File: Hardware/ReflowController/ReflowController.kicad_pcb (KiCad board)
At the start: 4 copper layers, 160 x 100 mm, 151 parts, among them J101 2060-1452, J102 2060-1452, J103 2060-1453, J104 2060-1452, J105 2060-1452, J106 2060-1452, J107 2060-1452, J108 2060-1452, J109 2060-1452, J110 2060-1452, J111 2060-1452, J112 2060-1452, J601 LCD_HEADER, Q601 BC848, SW601 RotaryEncoder_Switch, SW602 SW_UP, SW603 SW_DOWN, SW604 SW_LEFT, SW605 SW_RIGHT, SW606 SW_SELECT, SW607 SW_RET, SW608 SW_RESET, U301 TSR_1-2450, U302 LD1117S33TR_SOT223, U401 MAX31865xAP, U501 TB67H400AFNG, U601 PI4IOE5V6416, U701 VNQ5160K-E, U702 SZNUD3124DMT1G

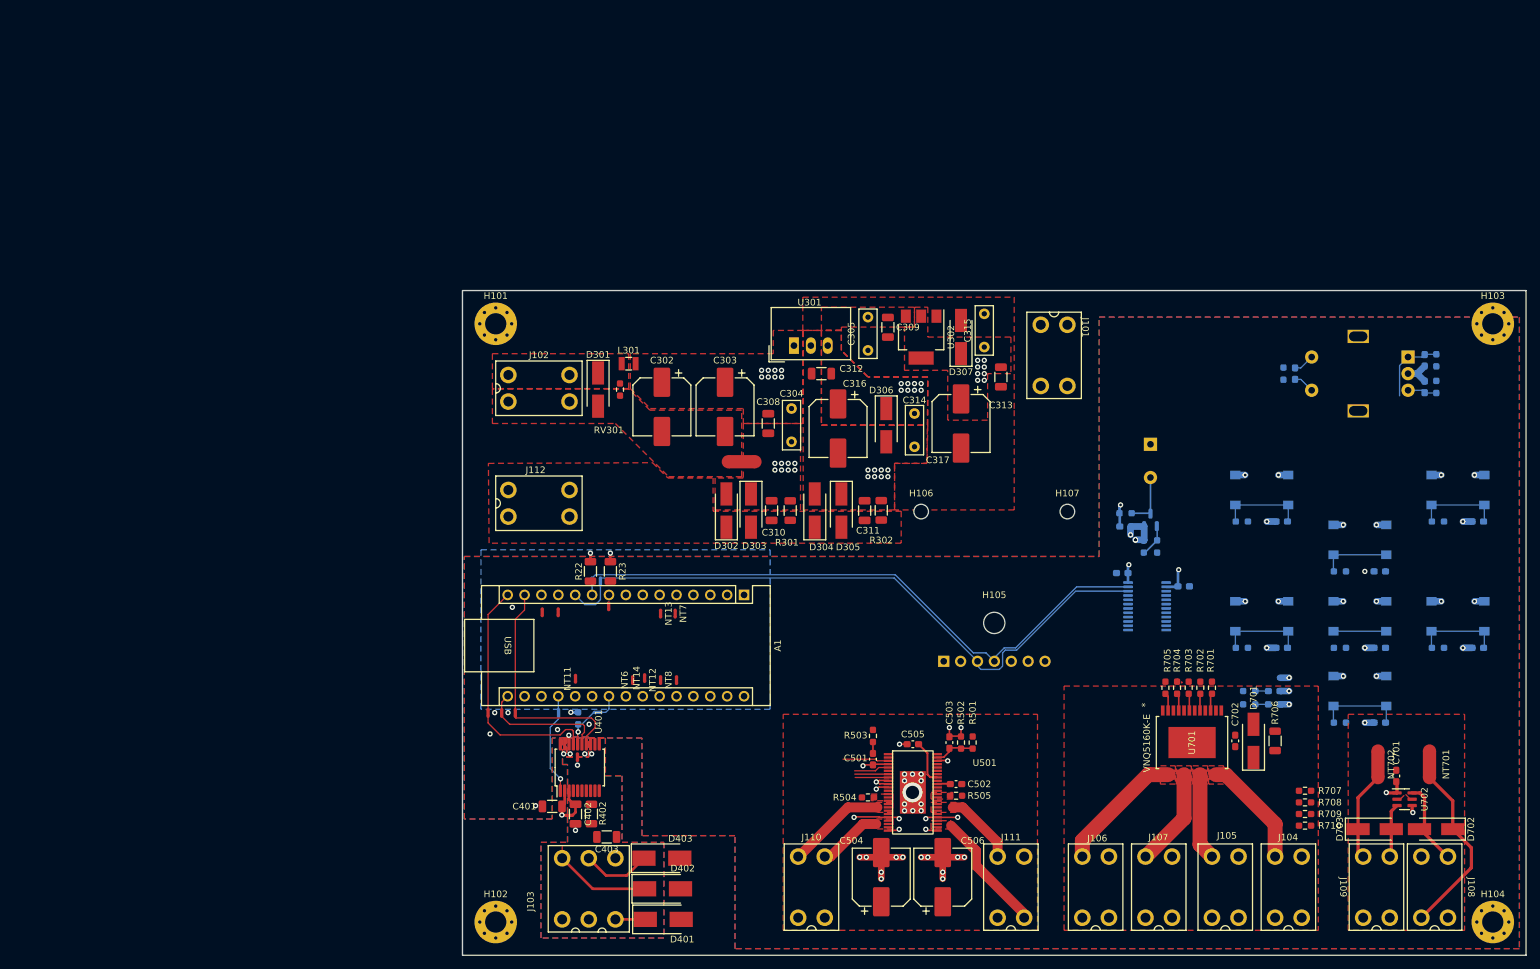
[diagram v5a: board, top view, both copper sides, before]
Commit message: work on +24V power
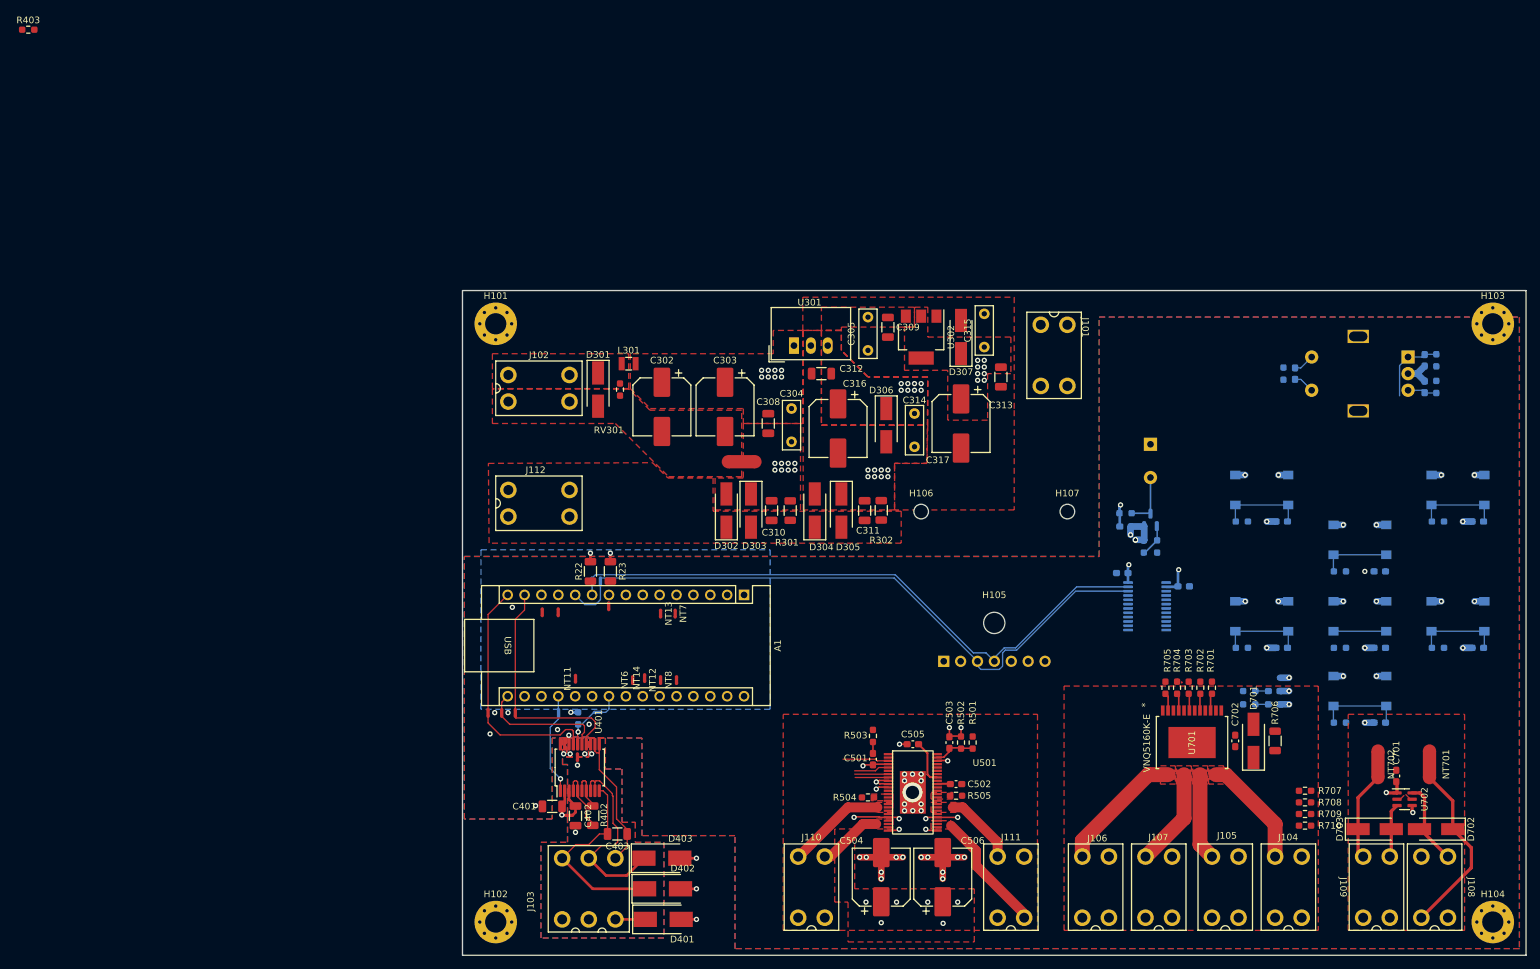
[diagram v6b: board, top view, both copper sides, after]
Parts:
- added R403: 10M, Resistor_SMD:R_0603_1608Metric_Pad0.98x0.95mm_HandSolder, F.Cu at (1.68, 0.76)
- moved C403 1.66 mm to (90.3, 121.8)
- moved R402 0.32 mm to (86.6, 119.0)
- moved C402 0.28 mm to (84.0, 119.0)
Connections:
- D401 pad 2: /TemperatureReader/T_AGND -> Earth
- D402 pad 2: /TemperatureReader/T_AGND -> Earth
- D403 pad 2: /TemperatureReader/T_AGND -> Earth
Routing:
- net /TemperatureReader/PT100_-IN: track 5.70 -> 26.0 mm
- net /TemperatureReader/PT100_+OUT: track 10.8 -> 30.4 mm
- net /TemperatureReader/PT100_+IN: track 16.1 -> 30.0 mm
- net /TemperatureReader/REFIN+: track 0.00 -> 9.39 mm
- net Earth: track 0.00 -> 7.20 mm, vias 0 -> 3
- net /TemperatureReader/REFIN-: track 0.00 -> 5.93 mm
- net +24V: vias 8 -> 14
- added copper zone on In2.Cu, net +24V

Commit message: wotk on on power and ground
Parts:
- moved R403 148.0 mm to (85.6, 122.6), turned to 180 degrees
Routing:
- net +3.3V: track 18.8 -> 270.0 mm
- net +24V: track 2.19 -> 116.1 mm
- net GNDPWR: track 45.3 -> 104.1 mm
- net /SDA: track 92.2 -> 47.1 mm
- net /SCL: track 91.5 -> 47.3 mm
- net /TemperatureReader/REFIN+: track 9.39 -> 12.3 mm
- added copper zone on In1.Cu, net /PSU/24V_GND_IN
- added copper zone on In1.Cu, net Earth
- removed copper zone on In2.Cu, net +3.3V

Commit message: work on layout
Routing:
- net +24V: track 116.1 -> 172.4 mm, vias 14 -> 22
- net GNDPWR: track 104.1 -> 95.6 mm, vias 41 -> 49
- removed copper zone on In2.Cu, net GNDPWR
